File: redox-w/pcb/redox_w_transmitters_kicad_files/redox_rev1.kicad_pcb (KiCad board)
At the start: 2 copper layers, 162.2 x 126.5 mm, 104 parts, among them K0 KEYSW, K1 KEYSW, K10 KEYSW, K11 KEYSW, K12 KEYSW, K13 KEYSW, K14 KEYSW, K15 KEYSW, K16 KEYSW, K2 KEYSW, K20 KEYSW, K21 KEYSW, K22 KEYSW, K23 KEYSW, K24 KEYSW, K25 KEYSW, K26 KEYSW, K3 KEYSW, K30 KEYSW, K31 KEYSW, K32 KEYSW, K33 KEYSW, K34 KEYSW, K35 KEYSW, K36 KEYSW, K4 KEYSW, K40 KEYSW, K41 KEYSW, K42 KEYSW, K43 KEYSW, K44 KEYSW, K45 KEYSW, K46 KEYSW, K5 KEYSW, K6 KEYSW

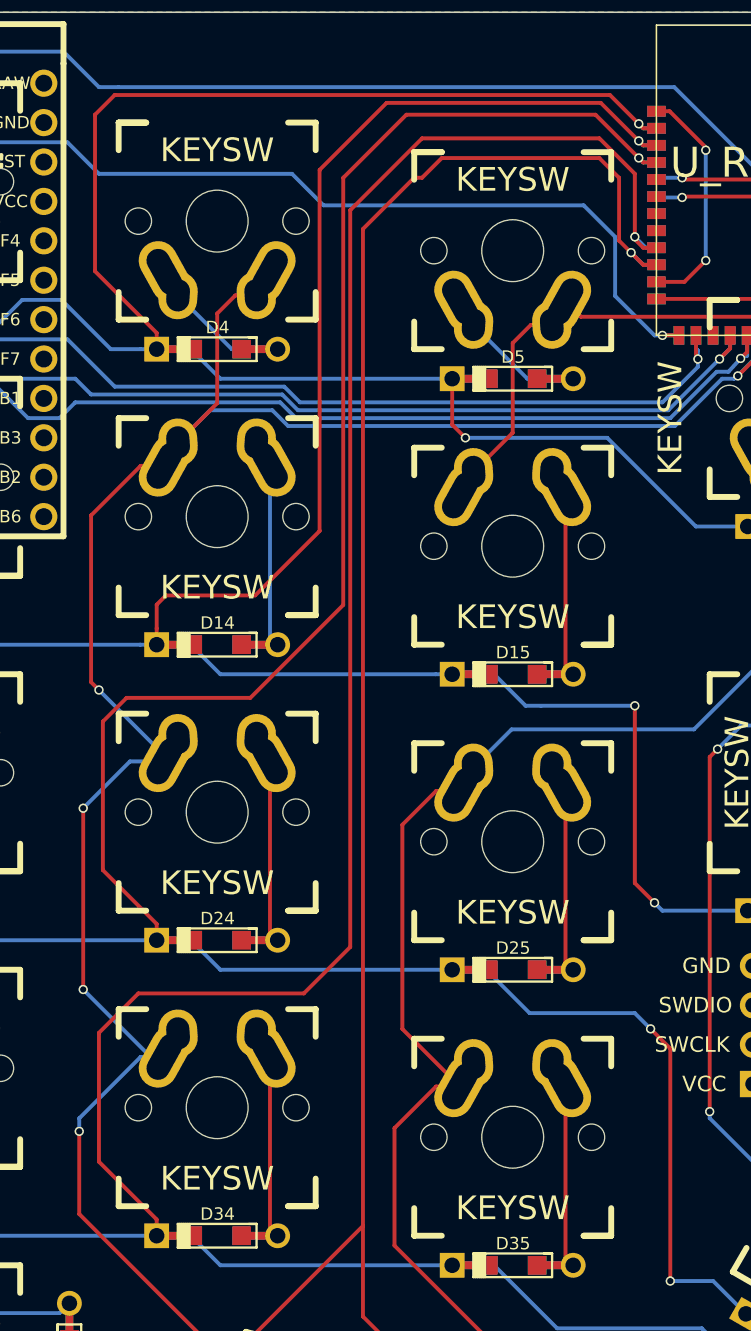
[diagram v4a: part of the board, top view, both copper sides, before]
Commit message: Moved Row Wiring On YJ To New Configuration
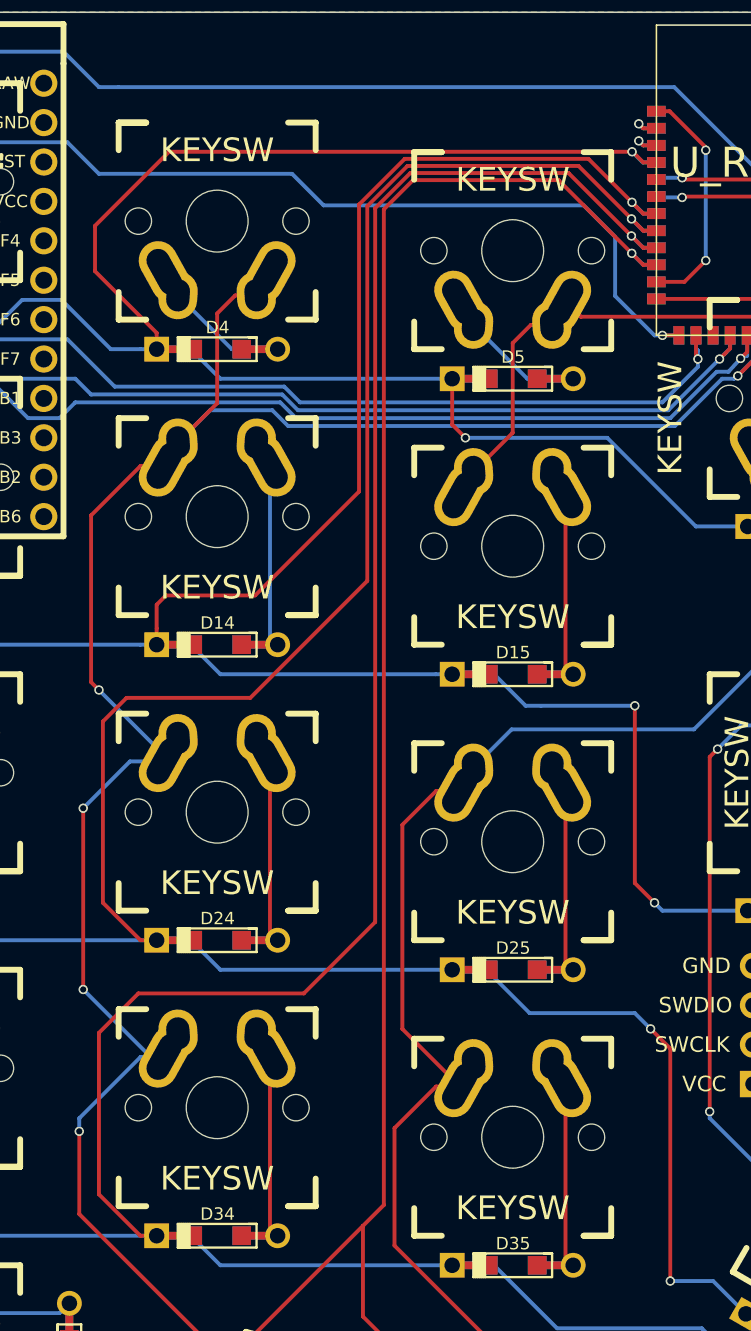
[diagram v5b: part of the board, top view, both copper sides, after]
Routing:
- net row0: track 183.2 -> 177.5 mm
- net row3: track 250.7 -> 246.3 mm
- net row4: track 226.8 -> 223.1 mm
- net row1: track 196.3 -> 193.0 mm
- net SDA1: track 0.00 -> 2.51 mm, vias 0 -> 1
- net SCL1: track 0.00 -> 2.51 mm, vias 0 -> 1
- net row2: track 223.4 -> 221.8 mm

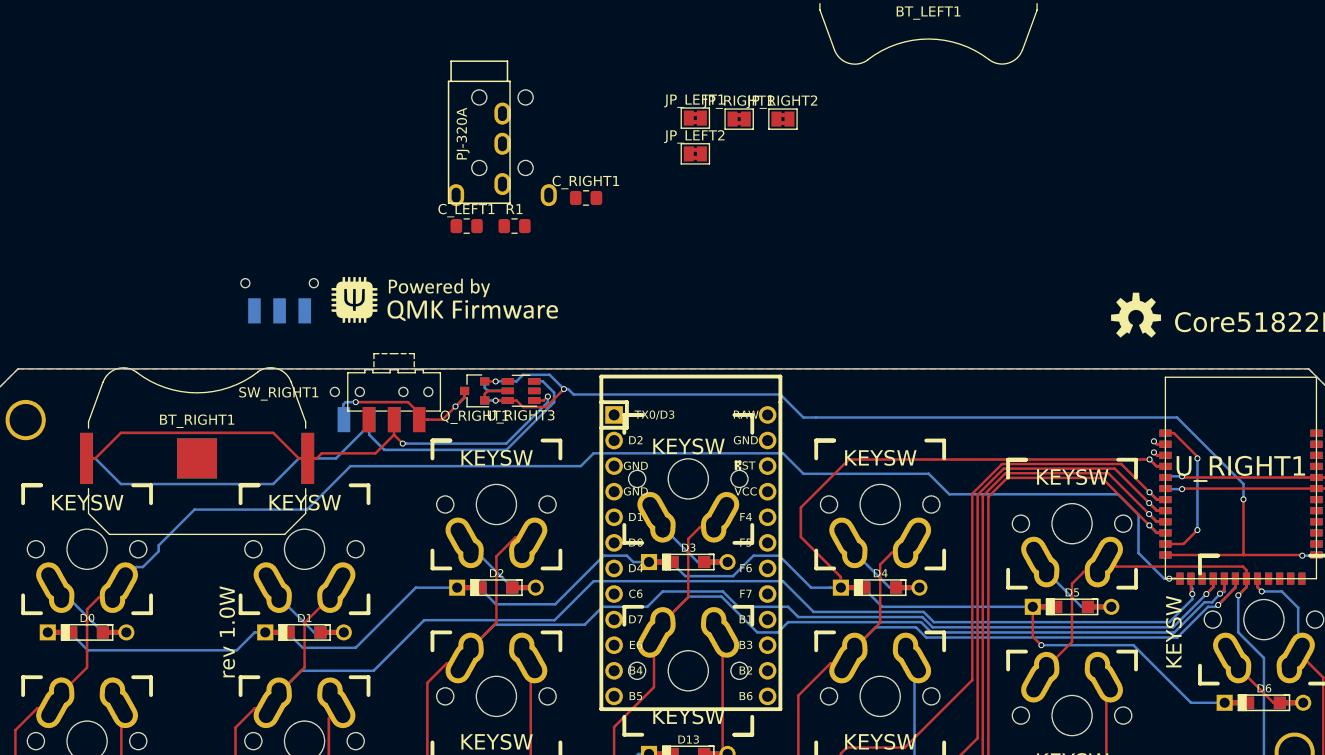
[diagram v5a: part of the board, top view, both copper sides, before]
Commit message: Renamed (Incorrectly) Named VCC0 Label To VCC1 And Rerouted Columns To Make Space For Headphone Jack
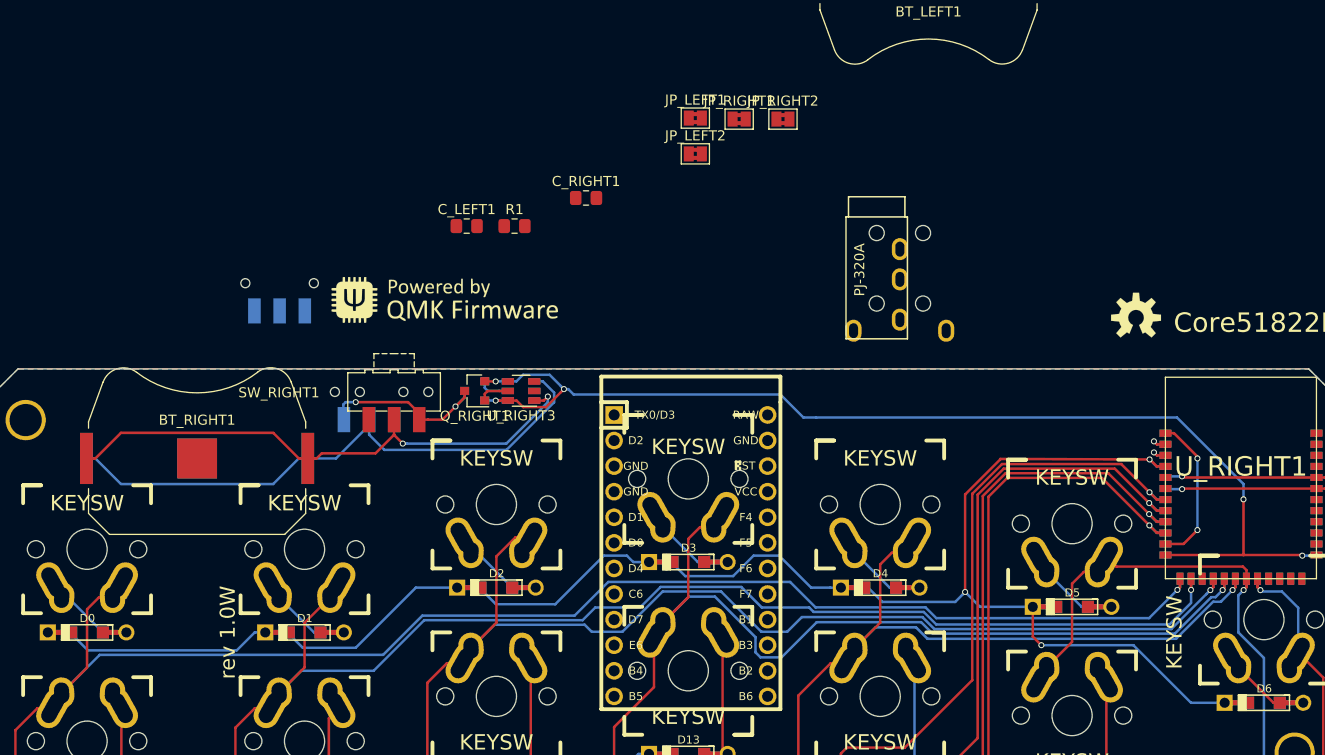
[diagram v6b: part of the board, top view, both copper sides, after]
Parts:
- moved TRRS1 41.7 mm to (172.1, 33.7)
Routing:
- net row0: track 177.5 -> 162.6 mm, vias 2 -> 3
- net col3: track 145.0 -> 147.3 mm
- net col4: track 137.5 -> 135.5 mm
- net col2: track 165.4 -> 166.8 mm
- net col0: track 202.6 -> 203.8 mm
- net col5: track 141.4 -> 140.7 mm
- net col1: track 181.5 -> 180.8 mm

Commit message: Imported Fixed Label From Previous Commit Into PCB
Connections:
- JP_LEFT1 pad 2: VCC0 -> VCC1
- JP_LEFT2 pad 2: VCC0 -> VCC1

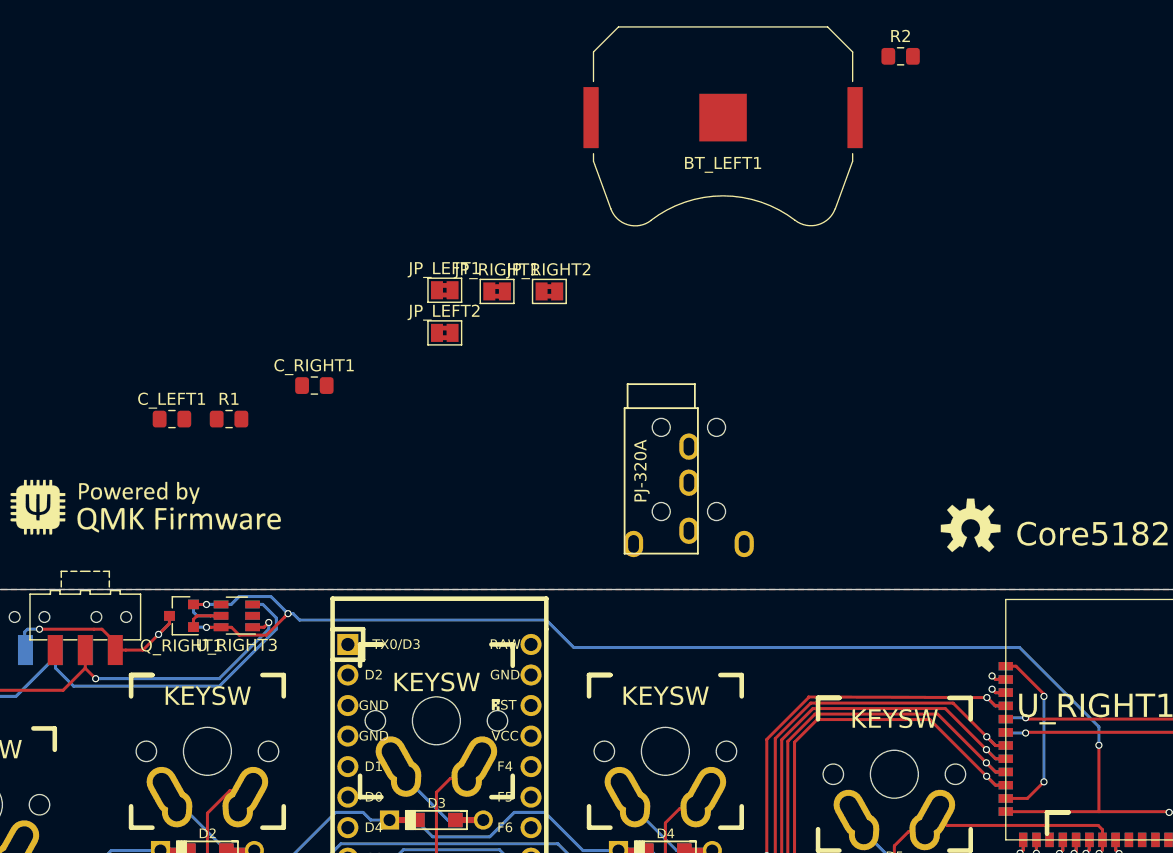
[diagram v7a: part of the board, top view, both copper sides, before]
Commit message: Emplaced Jumpers On PCB
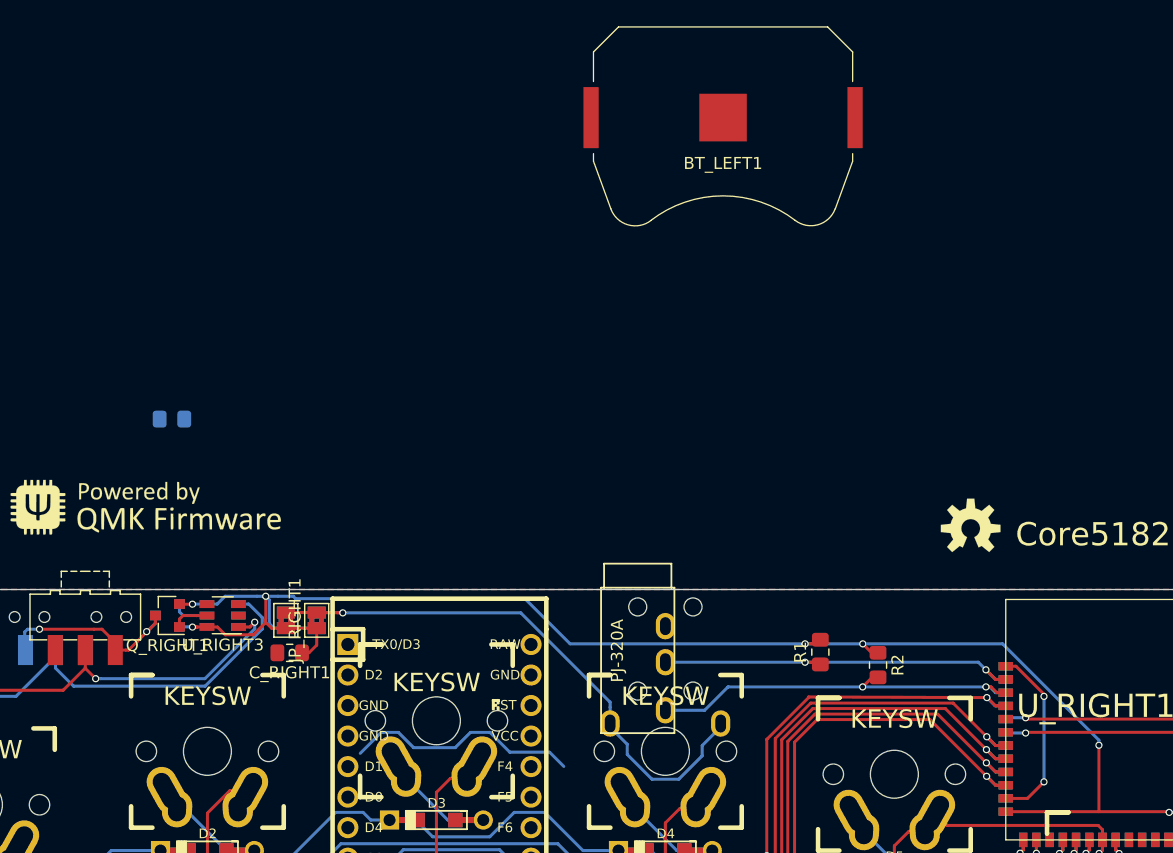
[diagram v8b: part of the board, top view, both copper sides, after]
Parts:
- C_LEFT1, JP_LEFT1, JP_LEFT2: moved to B.Cu
- moved R1 52.9 mm to (183.1, 54.0), turned to 90 degrees
- moved R2 50.7 mm to (187.9, 55.1), turned to 270 degrees
- moved JP_RIGHT2 35.1 mm to (138.6, 51.3), turned to 90 degrees
- moved JP_RIGHT1 31.2 mm to (141.2, 51.3), turned to 90 degrees
- moved JP_LEFT1 29.5 mm to (141.2, 51.3), turned to 90 degrees
- moved JP_LEFT2 27.3 mm to (138.6, 51.3), turned to 90 degrees
- moved C_RIGHT1 22.3 mm to (138.9, 54.0), turned to 180 degrees
- moved TRRS1 15.1 mm to (170.2, 48.6)
- moved U_LEFT2 1.17 mm to (133.3, 50.9)
- moved U_RIGHT3 1.17 mm to (133.4, 50.9)
- moved Q_LEFT1 1.17 mm to (128.8, 50.9)
- moved Q_RIGHT1 1.17 mm to (128.8, 50.9)
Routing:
- net VCC1: track 0.00 -> 51.0 mm, vias 0 -> 1
- net SCL1: track 2.51 -> 32.8 mm, vias 1 -> 2
- net SDA1: track 2.51 -> 32.2 mm, vias 1 -> 2
- net (no net): track 0.00 -> 19.9 mm
- net VCC: track 173.4 -> 192.0 mm, vias 5 -> 7
- net Net-(BT_LEFT1-Pad1): track 57.9 -> 56.8 mm
- net Net-(Q_RIGHT1-Pad3): track 16.3 -> 15.1 mm
- net Net-(BT_RIGHT1-Pad1): track 54.5 -> 53.4 mm
